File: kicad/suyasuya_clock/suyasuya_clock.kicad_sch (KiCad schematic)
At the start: 26 parts

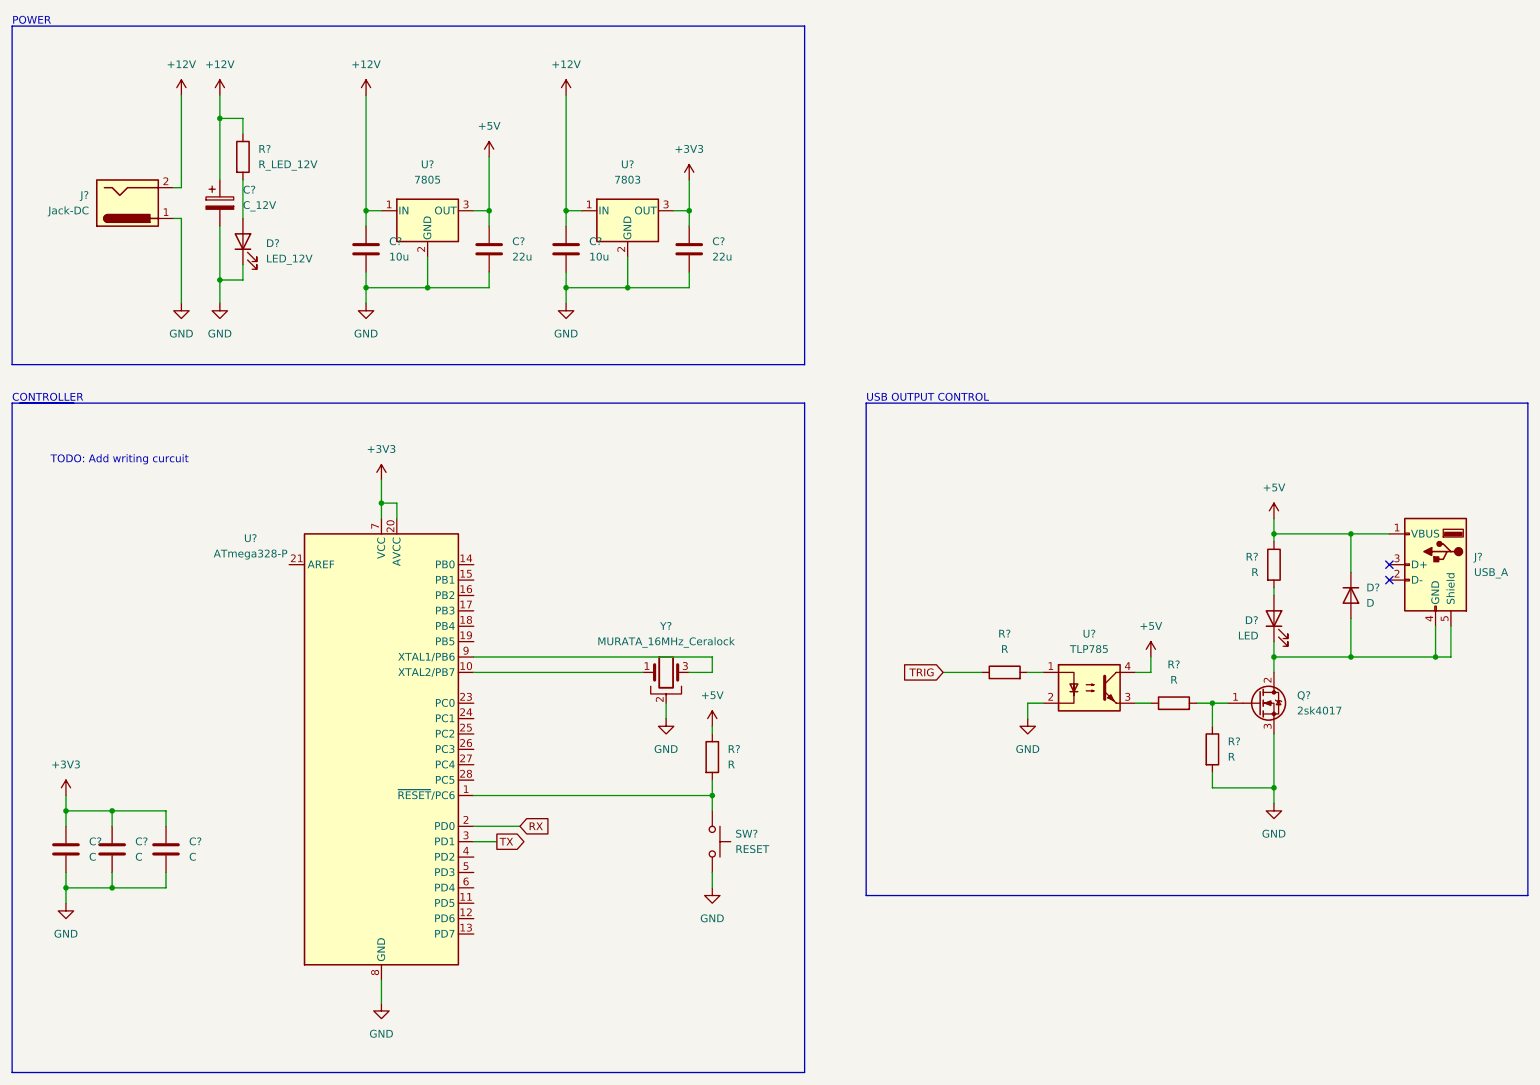
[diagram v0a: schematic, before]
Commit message: 書き込み回路を追加・周辺回路の微調整
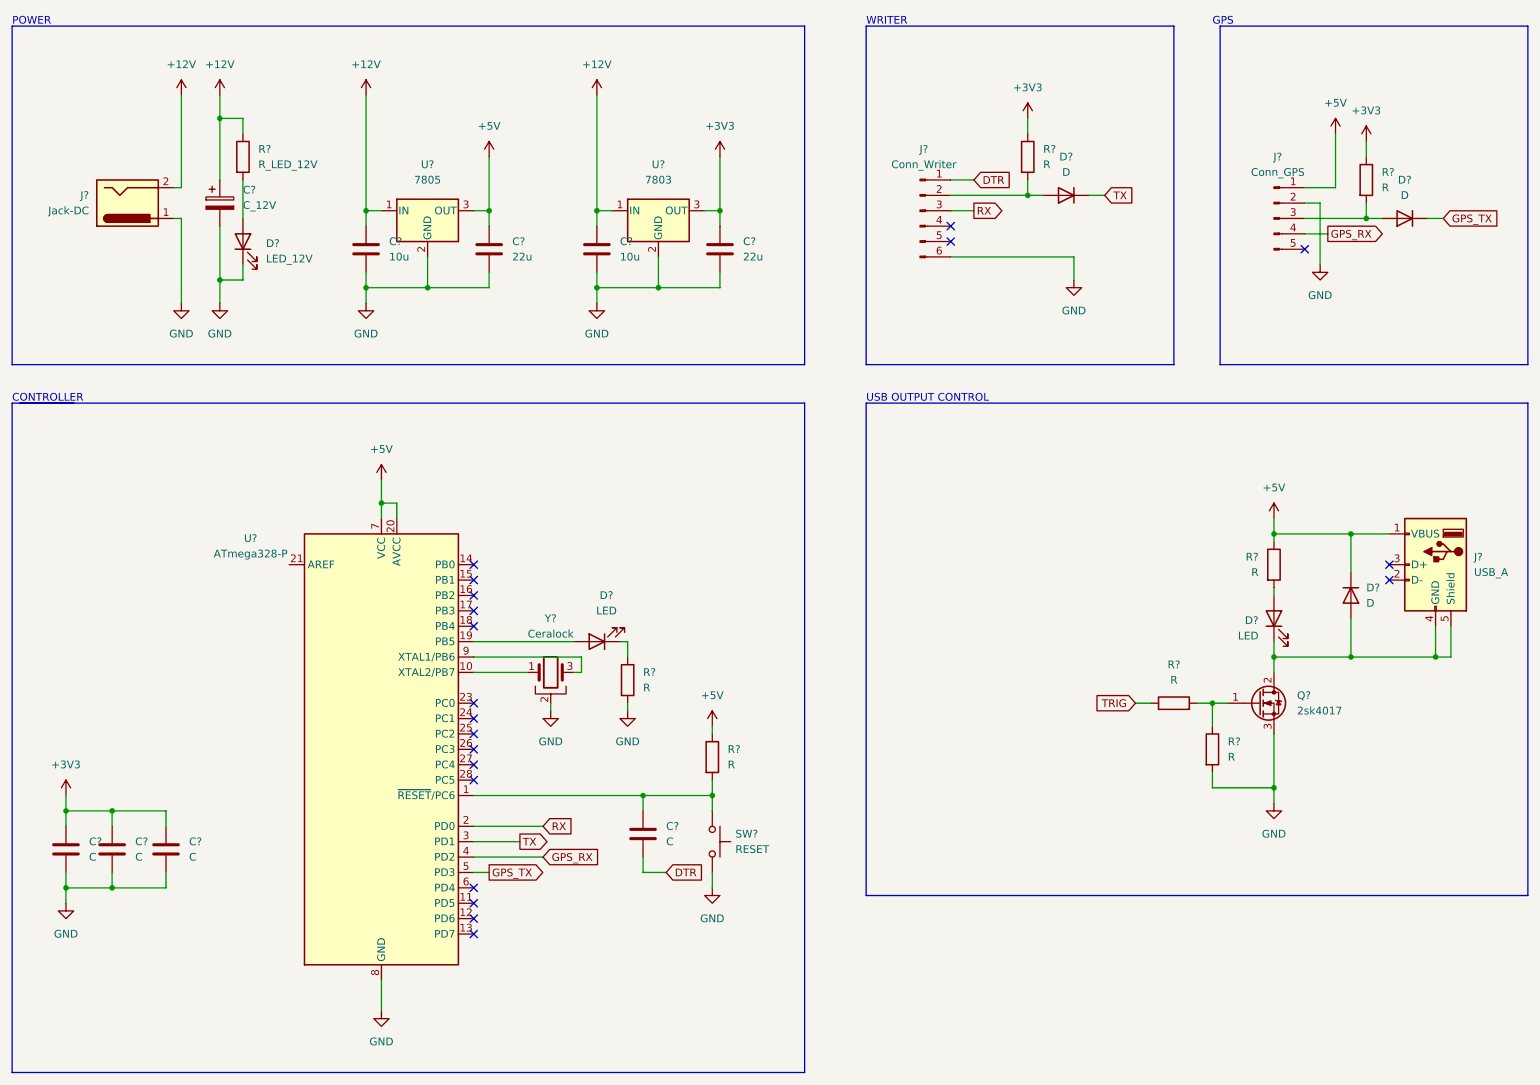
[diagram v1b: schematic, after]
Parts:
- removed C?: 10u, symbol Device:C
- removed C?: 22u, symbol Device:C
- removed R?: R, symbol Device:R
- removed U?: TLP785, Package_DIP:DIP-4_W7.62mm, symbol Isolator:TLP785
- removed U?: 7803, symbol Regulator_Linear:L7805
- added C?: 22u, symbol Device:C
- added C?: C, symbol Device:C
- added C?: 10u, symbol Device:C
- added D? (x2): D, symbol Device:D
- added D?: LED, symbol Device:LED
- added J?: Conn_GPS, symbol Connector:Conn_01x05_Male
- added J?: Conn_Writer, symbol Connector:Conn_01x06_Male
- added R? (x3): R, symbol Device:R
- added U?: 7803, symbol Regulator_Linear:L7805
- Y?: value MURATA_16MHz_Ceralock -> Ceralock
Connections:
- net +12V: now also C?.1, U?.1 (IN)
- net +3V3: now also C?.1, R?.1, R?.1, U?.3 (OUT); no longer U?.20 (AVCC), U?.7 (VCC)
- net +5V: now also U?.20 (AVCC), U?.7 (VCC), J?.1 (Pin_1)
- net GND: now also C?.2, C?.2, J?.2 (Pin_2), J?.6 (Pin_6), R?.2, U?.2 (GND)
- net RX: now also J?.3 (Pin_3)
- net TRIG: now also R?.1
- net TX: now also D?.1 (K)
- net at R?.2, SW?.1, U?.1 (~{RESET}/PC6): now also C?.1
- net at U?.19 (PB5): now also D?.2 (A)
- net GPS_RX: now reaches U?.4 (PD2)
- net GPS_RX: now also J?.4 (Pin_4)
- net GPS_TX: now reaches U?.5 (PD3)
- net GPS_TX: now also D?.1 (K)
- new net: D?.2 (A), J?.2 (Pin_2), R?.2
- new net: D?.2 (A), J?.3 (Pin_3), R?.2
- new net: D?.1 (K), R?.1
- new net DTR: C?.2, J?.1 (Pin_1)
- no-connect marks 2 -> 20
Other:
- note added: "GPS"
- note added: "WRITER"
- note removed: "TODO: Add writing curcuit"
- moved on the sheet: Y?

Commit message: 電源回路調整・出力実装
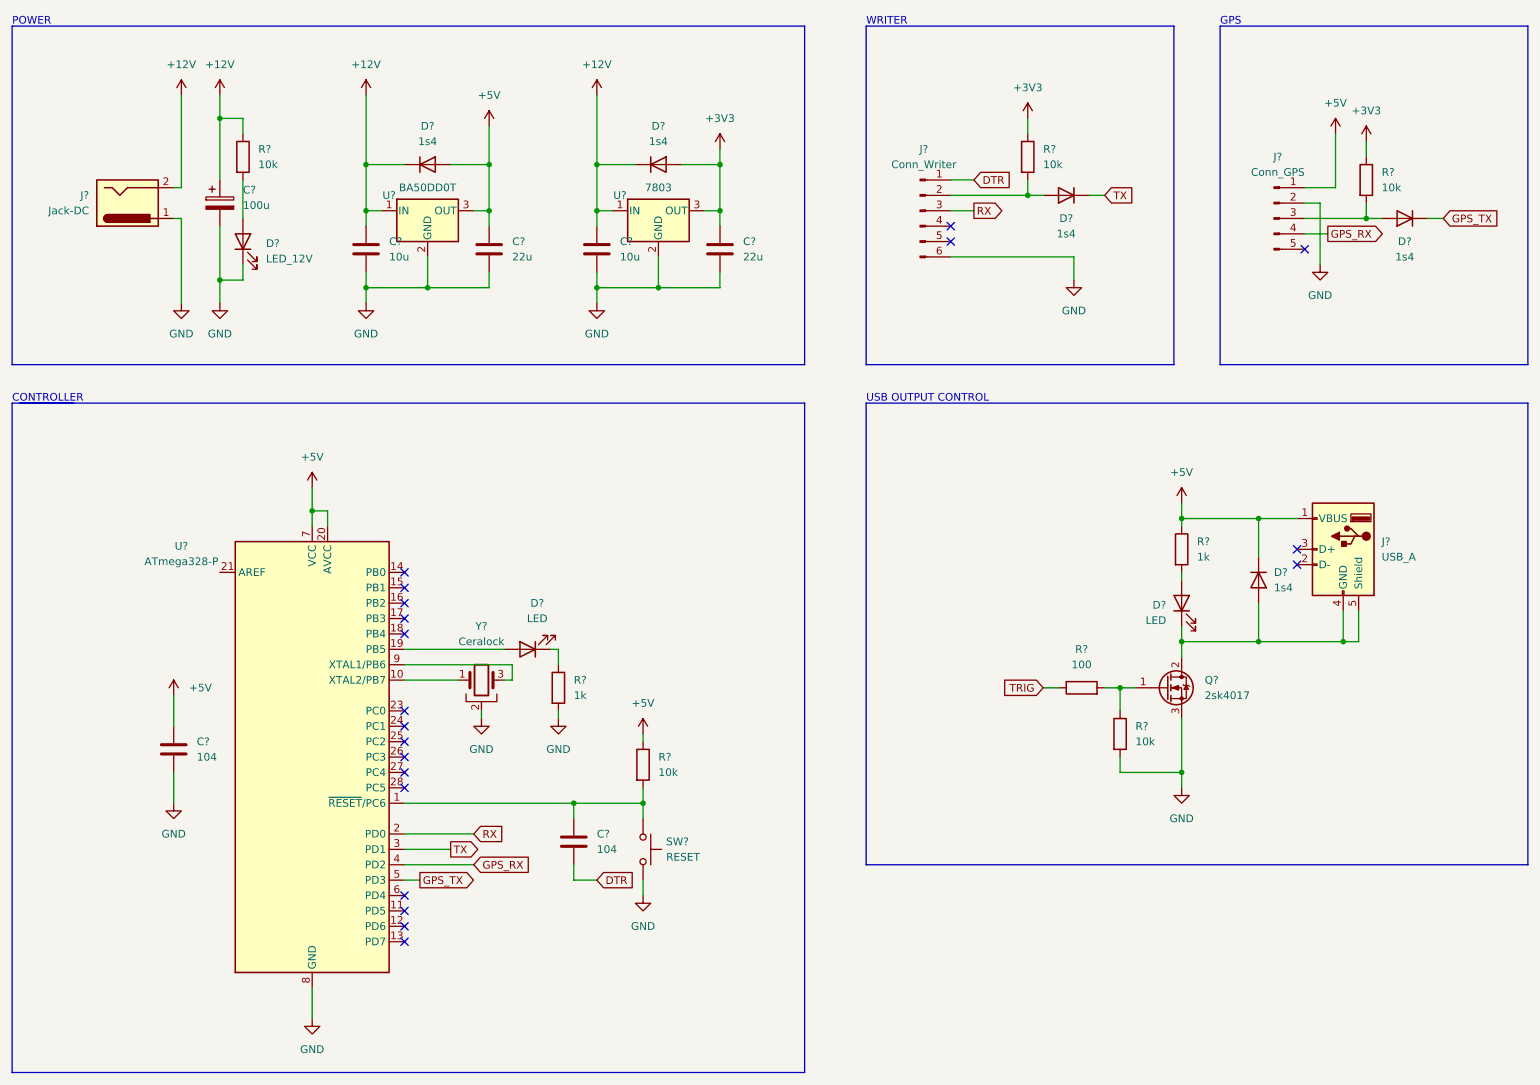
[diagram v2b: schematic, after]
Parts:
- removed C? (x2): C, symbol Device:C
- added D? (x2): 1s4, symbol Device:D
- C? (x2): value C -> 104
- C?: value C_12V -> 100u
- D? (x3): value D -> 1s4
- R? (x4): value R -> 10k
- R? (x2): value R -> 1k
- R?: value R_LED_12V -> 10k
- R?: value R -> 100
- U?: value 7805 -> BA50DD0T
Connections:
- net +12V: now also D?.1 (K), D?.1 (K)
- net +3V3: now also D?.2 (A); no longer C?.1
- net +5V: now also C?.1, D?.2 (A)
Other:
- moved on the sheet: C?, D?, J?, Q?, R?, SW?, U?, Y?

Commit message: 基板図を書いた・回路の細かな修正
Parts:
- removed J?: USB_A, symbol Connector:USB_A
- added J4: USB_OUTPUT, Connector_PinHeader_2.54mm:PinHeader_1x04_P2.54mm_Vertical, symbol Connector:Conn_01x04_Female
- C1, C5: renamed from C?; footprint (none) -> Capacitor_THT:C_Disc_D4.3mm_W1.9mm_P5.00mm
- C2: renamed from C?; footprint (none) -> Capacitor_THT:CP_Radial_D8.0mm_P2.50mm
- C3, C4, C6, C7: renamed from C?; footprint (none) -> Capacitor_THT:CP_Radial_D5.0mm_P2.50mm
- D1, D3, D6: renamed from D?; footprint (none) -> LED_THT:LED_D3.0mm
- D2, D4, D5, D7, D8: renamed from D?; footprint (none) -> Diode_THT:D_A-405_P7.62mm_Horizontal
- J1: renamed from J?; footprint (none) -> Connector_BarrelJack:BarrelJack_CUI_PJ-102AH_Horizontal
- J2: renamed from J?; footprint (none) -> Connector_PinHeader_2.54mm:PinHeader_1x06_P2.54mm_Vertical
- J3: renamed from J?; footprint (none) -> Connector_PinHeader_2.54mm:PinHeader_1x05_P2.54mm_Vertical
- Q1: renamed from Q?; footprint (none) -> Package_TO_SOT_THT:TO-251-3_Vertical
- R1, R2, R3, R4, R5, R6, R7, R8: renamed from R?; footprint (none) -> Resistor_THT:R_Axial_DIN0207_L6.3mm_D2.5mm_P10.16mm_Horizontal
- SW1: renamed from SW?; footprint (none) -> Button_Switch_THT:SW_PUSH_6mm
- U2, U3: renamed from U?; footprint (none) -> Package_TO_SOT_THT:TO-220-3_Vertical
- Y1: renamed from Y?; footprint (none) -> Connector_PinHeader_2.54mm:PinHeader_1x03_P2.54mm_Vertical
- gave numbers to parts that had none: 1
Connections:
- net +12V: now also J1.1; no longer J1.2
- net +5V: now also J4.1 (Pin_1)
- net GND: now also J1.2; no longer J1.1
- net TRIG: now also U1.15 (PB1)
- net at D6.1 (K), D7.2 (A), Q1.2 (D): now also J4.4 (Pin_4)
- no-connect marks 20 -> 19

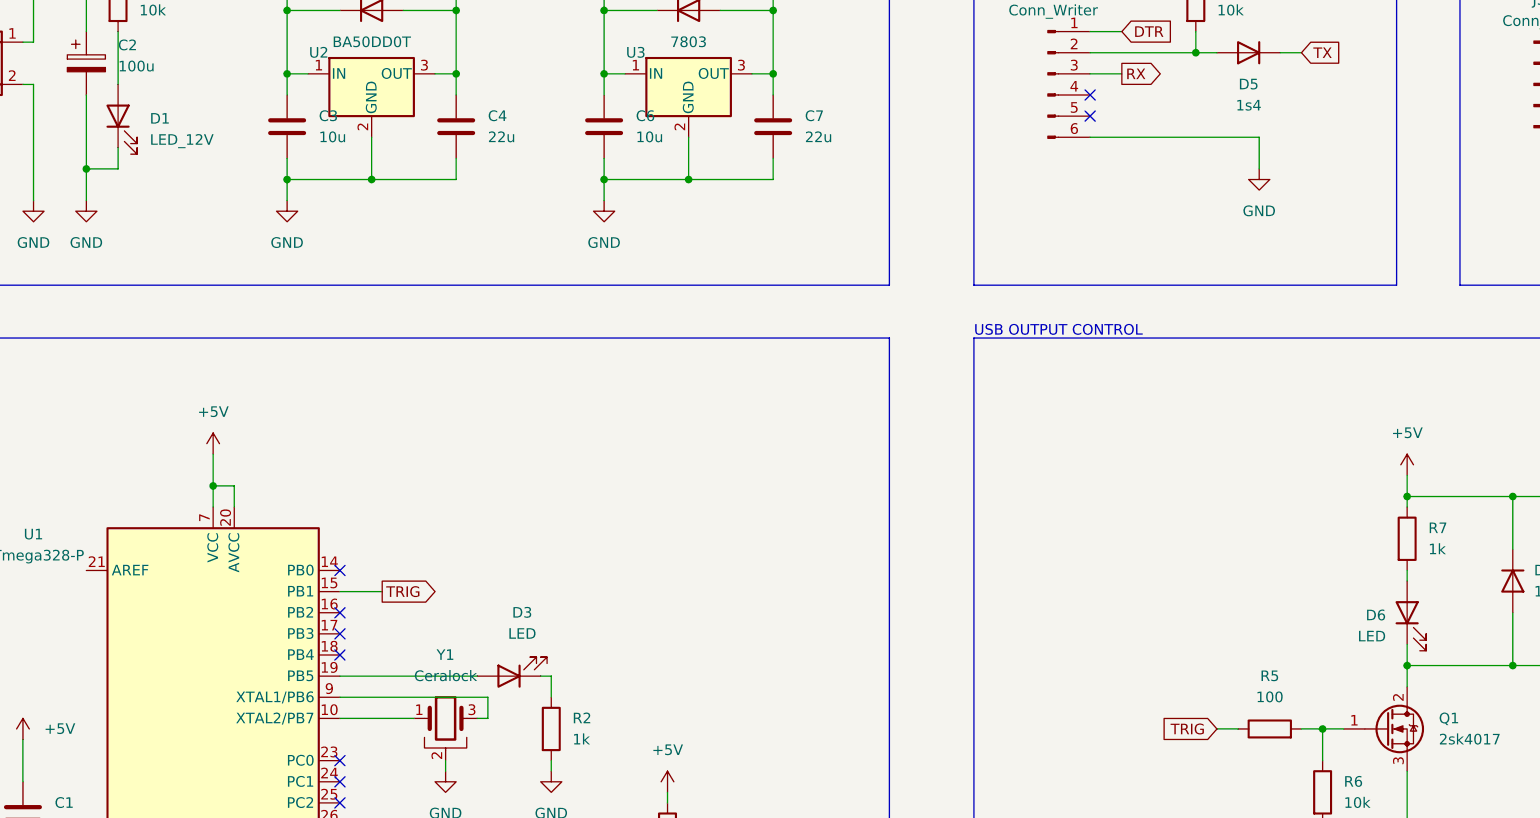
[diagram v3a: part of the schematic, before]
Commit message: ファーム変更・回路修正
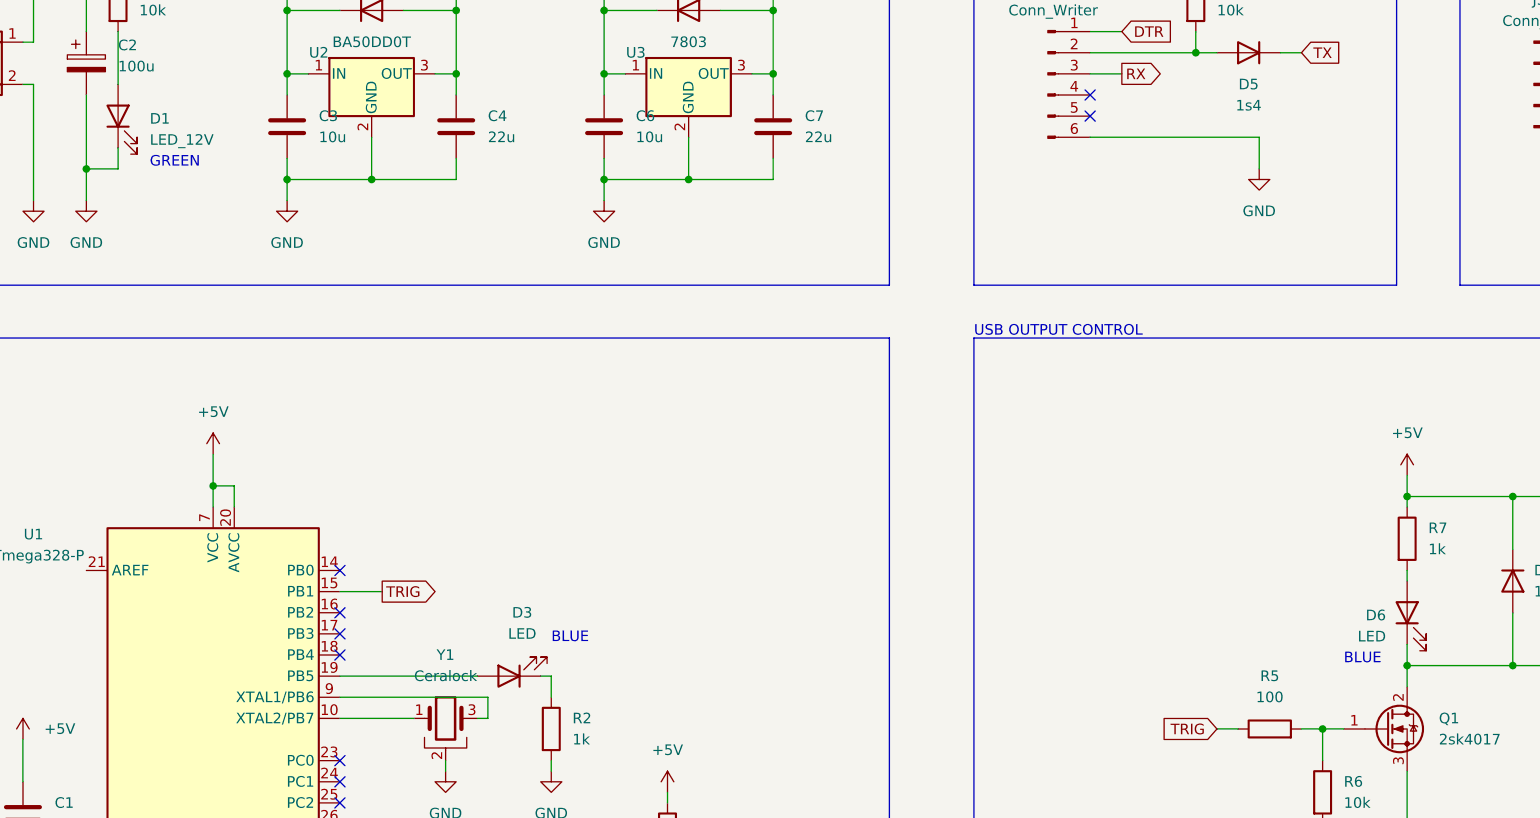
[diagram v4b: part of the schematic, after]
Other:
- note added: "BLUE"
- note added: "GREEN"
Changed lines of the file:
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@@
+    (effects (font (size 1.27 1.27)) (justify left bottom))
+  )
+  (text "GREEN" (at 69.85 62.23 0)
     (effects (font (size 1.27 1.27)) (justify left bottom))
   )
@@
     (effects (font (size 1.27 1.27)) (justify left bottom))
   )
+  (text "BLUE" (at 118.11 119.38 0)
+    (effects (font (size 1.27 1.27)) (justify left bottom))
+  )
+  (text "BLUE" (at 213.36 121.92 0)
+    (effects (font (size 1.27 1.27)) (justify left bottom))
+  )
